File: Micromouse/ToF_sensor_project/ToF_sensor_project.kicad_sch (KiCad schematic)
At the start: 6 parts, among them J3 Conn_01x03_Pin

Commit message: Schematic overhaul
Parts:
- removed C2: 22 µF, Capacitor_SMD:C_0402_1005Metric, symbol Device:C
- removed Cin_VR1: 10 µF, Capacitor_SMD:C_0402_1005Metric, symbol Device:C
- removed J3: Conn_01x03_Pin, Connector_JST:JST_ZH_B3B-ZR_1x03_P1.50mm_Vertical, symbol Connector:Conn_01x03_Pin
- removed Renb1: 30kΩ, Resistor_SMD:R_0603_1608Metric, symbol Device:R
- removed Rent1: 62kΩ, Resistor_SMD:R_0603_1608Metric, symbol Device:R
- removed VR1: TPSM861253RDXR, MM_TPSM861253RDXR:TPSM861253RDXR, symbol TPSM861253RDXR:TPSM861253RDXR
- added C11: 100n, Capacitor_SMD:C_0603_1608Metric, symbol Device:C
- added C9: 4.7u, Capacitor_SMD:C_0603_1608Metric, symbol Device:C
- added J2: Conn_01x06_Pin, symbol Connector:Conn_01x06_Pin
- added R3, R4: 10k, Resistor_SMD:R_0603_1608Metric, symbol Device:R
- added U1: VL53L1CXV0FY1, MM_VL53L4CDV0DH-1:LGA12_STM, symbol Sensor_Distance:VL53L1CXV0FY1
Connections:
- net GND: now also C11.1, C9.1, J2.6 (Pin_6), U1.12 (GND), U1.2 (AVSSVCSEL), U1.3 (GND), U1.4 (GND), U1.6 (GND)
- new net: J2.4 (Pin_4), U1.10 (SCL)
- new net: J2.5 (Pin_5), R4.2, U1.5 (XSHUT)
- new net: J2.2 (Pin_2), R3.2, U1.7 (GPIO1)
- new net: J2.3 (Pin_3), U1.9 (SDA)
- new net +3.3V: C11.2, C9.2, J2.1 (Pin_1), R3.1, R4.1, U1.1 (AVDDVCSEL), U1.11 (AVDD)
- no-connect marks 1 -> 0
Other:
- note added: "+3.3V INT SDA SCL XSHUT GND"
- note added: "I2C lines are pulled up on main schematic"

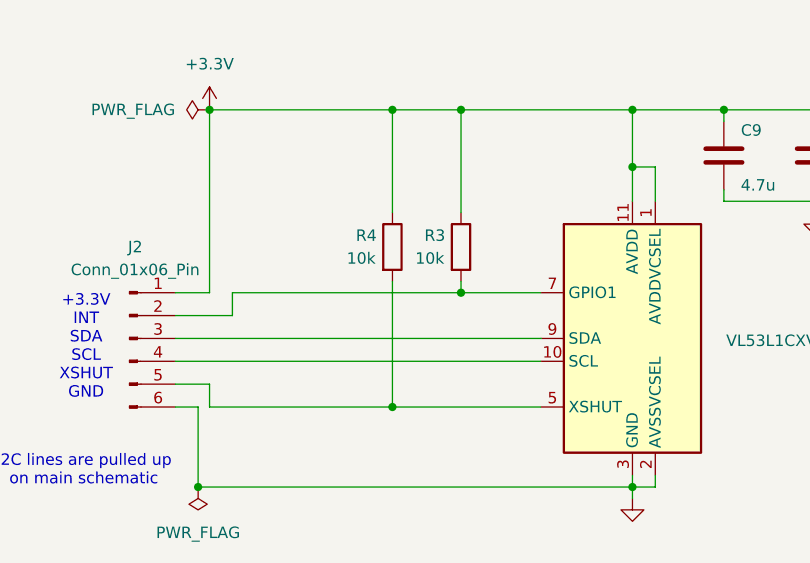
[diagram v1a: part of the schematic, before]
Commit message: Cleaned up layout
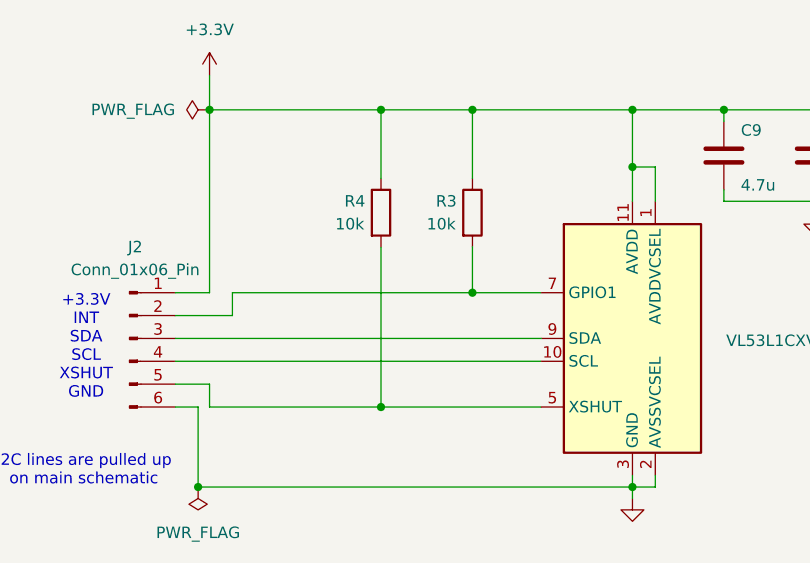
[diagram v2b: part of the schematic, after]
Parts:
- J2: footprint (none) -> Connector_PinHeader_2.00mm:PinHeader_1x06_P2.00mm_Vertical
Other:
- moved on the sheet: R3, R4
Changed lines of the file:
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@@
-	)
-	(junction
-		(at 86.36 77.47)
-		(diameter 0)
-		(color 0 0 0 0)
 	)
 	(junction
@@
 	)
 	(junction
-		(at 93.98 64.77)
+		(at 85.09 44.45)
 		(diameter 0)
 		(color 0 0 0 0)
@@
 	)
 	(junction
+		(at 85.09 77.47)
+		(diameter 0)
+		(color 0 0 0 0)
+	)
+	(junction
 		(at 113.03 86.36)
 		(diameter 0)
@@
 	)
 	(junction
-		(at 93.98 44.45)
+		(at 95.25 64.77)
 		(diameter 0)
 		(color 0 0 0 0)
 	)
 	(junction
-		(at 86.36 44.45)
+		(at 95.25 44.45)
 		(diameter 0)
 		(color 0 0 0 0)
@@
 	(wire
 		(pts
+			(xy 85.09 44.45) (xy 95.25 44.45)
+		)
+		(stroke
+			(width 0)
+			(type default)
+		)
+	)
+	(wire
+		(pts
 			(xy 133.35 53.34) (xy 133.35 54.61)
 		)
@@
 	(wire
 		(pts
-			(xy 93.98 63.5) (xy 93.98 64.77)
+			(xy 95.25 59.69) (xy 95.25 64.77)
 		)
 		(stroke
@@
 	(wire
 		(pts
+			(xy 85.09 77.47) (xy 102.87 77.47)
+		)
+		(stroke
+			(width 0)
+			(type default)
+		)
+	)
+	(wire
+		(pts
 			(xy 115.57 86.36) (xy 115.57 85.09)
 		)
@@
 	(wire
 		(pts
+			(xy 95.25 64.77) (xy 102.87 64.77)
+		)
+		(stroke
+			(width 0)
+			(type default)
+		)
+	)
+	(wire
+		(pts
 			(xy 66.04 64.77) (xy 62.23 64.77)
 		)
@@
 	(wire
 		(pts
-			(xy 66.04 77.47) (xy 86.36 77.47)
+			(xy 66.04 77.47) (xy 85.09 77.47)
 		)
 		(stroke
@@
 	(wire
 		(pts
-			(xy 86.36 77.47) (xy 102.87 77.47)
-		)
-		(stroke
-			(width 0)
-			(type default)
-		)
-	)
-	(wire
-		(pts
-			(xy 86.36 44.45) (xy 113.03 44.45)
-		)
-		(stroke
-			(width 0)
-			(type default)
-		)
-	)
-	(wire
-		(pts
-			(xy 93.98 64.77) (xy 102.87 64.77)
-		)
-		(stroke
-			(width 0)
-			(type default)
-		)
-	)
-	(wire
-		(pts
 			(xy 62.23 69.85) (xy 102.87 69.85)
 		)
@@
 	(wire
 		(pts
-			(xy 68.58 64.77) (xy 93.98 64.77)
-		)
-		(stroke
-			(width 0)
-			(type default)
-		)
-	)
-	(wire
-		(pts
-			(xy 93.98 44.45) (xy 93.98 55.88)
+			(xy 68.58 64.77) (xy 95.25 64.77)
+		)
+		(stroke
+			(width 0)
+			(type default)
+		)
+	)
+	(wire
+		(pts
+			(xy 95.25 44.45) (xy 95.25 52.07)
 		)
 		(stroke
@@
 	(wire
 		(pts
+			(xy 66.04 40.64) (xy 66.04 44.45)
+		)
+		(stroke
+			(width 0)
+			(type default)
+		)
+	)
+	(wire
+		(pts
 			(xy 123.19 44.45) (xy 133.35 44.45)
 		)
@@
 	(wire
 		(pts
-			(xy 66.04 44.45) (xy 86.36 44.45)
+			(xy 66.04 44.45) (xy 85.09 44.45)
+		)
+		(stroke
+			(width 0)
+			(type default)
+		)
+	)
+	(wire
+		(pts
+			(xy 95.25 44.45) (xy 113.03 44.45)
 		)
 		(stroke
@@
 	(wire
 		(pts
-			(xy 86.36 63.5) (xy 86.36 77.47)
+			(xy 85.09 59.69) (xy 85.09 77.47)
 		)
 		(stroke
@@
 	(wire
 		(pts
-			(xy 86.36 44.45) (xy 86.36 55.88)
+			(xy 85.09 44.45) (xy 85.09 52.07)
 		)
 		(stroke
@@
 	(symbol
 		(lib_id "power:+3.3V")
-		(at 66.04 44.45 0)
+		(at 66.04 40.64 0)
 		(unit 1)
 		(body_style 1)
@@
 		(fields_autoplaced yes)
 		(property "Reference" "#PWR01"
-			(at 66.04 48.26 0)
+			(at 66.04 44.45 0)
 			(hide yes)
 			(show_name no)
@@
 		)
 		(property "Value" "+3.3V"
-			(at 66.04 39.37 0)
+			(at 66.04 35.56 0)
 			(show_name no)
 			(do_not_autoplace no)
@@
 		)
 		(property "Footprint" ""
-			(at 66.04 44.45 0)
+			(at 66.04 40.64 0)
 			(hide yes)
 			(show_name no)
@@
 		)
 		(property "Datasheet" ""
-			(at 66.04 44.45 0)
+			(at 66.04 40.64 0)
 			(hide yes)
 			(show_name no)
@@
 		)
 		(property "Description" "Power symbol creates a global label with name \"+3.3V\""
-			(at 66.04 44.45 0)
+			(at 66.04 40.64 0)
 			(hide yes)
 			(show_name no)
@@
 	(symbol
 		(lib_id "Device:R")
-		(at 93.98 59.69 0)
+		(at 95.25 55.88 0)
 		(unit 1)
 		(body_style 1)
@@
 		(dnp no)
 		(property "Reference" "R3"
-			(at 89.916 58.42 0)
+			(at 91.186 54.61 0)
 			(show_name no)
 			(do_not_autoplace no)
@@
 		)
 		(property "Value" "10k"
-			(at 88.9 60.96 0)
+			(at 90.17 57.15 0)
 			(show_name no)
 			(do_not_autoplace no)
@@
 		)
 		(property "Footprint" "Resistor_SMD:R_0603_1608Metric"
-			(at 92.202 59.69 90)
+			(at 93.472 55.88 90)
 			(hide yes)
 			(show_name no)
@@
 		)
 		(property "Datasheet" ""
-			(at 93.98 59.69 0)
+			(at 95.25 55.88 0)
 			(hide yes)
 			(show_name no)
@@
 		)
 		(property "Description" "Resistor"
-			(at 93.98 59.69 0)
+			(at 95.25 55.88 0)
 			(hide yes)
 			(show_name no)
@@
 		)
 		(property "Availability" ""
-			(at 93.98 59.69 0)
+			(at 95.25 55.88 0)
 			(hide yes)
 			(show_name no)
@@
 		)
 		(property "Check_prices" ""
-			(at 93.98 59.69 0)
+			(at 95.25 55.88 0)
 			(hide yes)
 			(show_name no)
@@
 		)
 		(property "Description_1" ""
-			(at 93.98 59.69 0)
+			(at 95.25 55.88 0)
 			(hide yes)
 			(show_name no)
@@
 		)
 		(property "MF" ""
-			(at 93.98 59.69 0)
+			(at 95.25 55.88 0)
 			(hide yes)
 			(show_name no)
@@
 		)
 		(property "MP" ""
-			(at 93.98 59.69 0)
+			(at 95.25 55.88 0)
 			(hide yes)
 			(show_name no)
@@
 		)
 		(property "Package" ""
-			(at 93.98 59.69 0)
+			(at 95.25 55.88 0)
 			(hide yes)
 			(show_name no)
@@
 		)
 		(property "Price" ""
-			(at 93.98 59.69 0)
+			(at 95.25 55.88 0)
 			(hide yes)
 			(show_name no)
@@
 		)
 		(property "SnapEDA_Link" ""
-			(at 93.98 59.69 0)
+			(at 95.25 55.88 0)
 			(hide yes)
 			(show_name no)
@@
 	(symbol
 		(lib_id "Device:R")
-		(at 86.36 59.69 0)
+		(at 85.09 55.88 0)
 		(unit 1)
 		(body_style 1)
@@
 		(dnp no)
 		(property "Reference" "R4"
-			(at 82.296 58.42 0)
+			(at 81.026 54.61 0)
 			(show_name no)
 			(do_not_autoplace no)
@@
 		)
 		(property "Value" "10k"
-			(at 81.28 60.96 0)
+			(at 80.01 57.15 0)
 			(show_name no)
 			(do_not_autoplace no)
@@
 		)
 		(property "Footprint" "Resistor_SMD:R_0603_1608Metric"
-			(at 84.582 59.69 90)
+			(at 83.312 55.88 90)
 			(hide yes)
 			(show_name no)
@@
 		)
 		(property "Datasheet" ""
-			(at 86.36 59.69 0)
+			(at 85.09 55.88 0)
 			(hide yes)
 			(show_name no)
@@
 		)
 		(property "Description" "Resistor"
-			(at 86.36 59.69 0)
+			(at 85.09 55.88 0)
 			(hide yes)
 			(show_name no)
@@
 		)
 		(property "Availability" ""
-			(at 86.36 59.69 0)
+			(at 85.09 55.88 0)
 			(hide yes)
 			(show_name no)
@@
 		)
 		(property "Check_prices" ""
-			(at 86.36 59.69 0)
+			(at 85.09 55.88 0)
 			(hide yes)
 			(show_name no)
@@
 		)
 		(property "Description_1" ""
-			(at 86.36 59.69 0)
+			(at 85.09 55.88 0)
 			(hide yes)
 			(show_name no)
@@
 		)
 		(property "MF" ""
-			(at 86.36 59.69 0)
+			(at 85.09 55.88 0)
 			(hide yes)
 			(show_name no)
@@
 		)
 		(property "MP" ""
-			(at 86.36 59.69 0)
+			(at 85.09 55.88 0)
 			(hide yes)
 			(show_name no)
@@
 		)
 		(property "Package" ""
-			(at 86.36 59.69 0)
+			(at 85.09 55.88 0)
 			(hide yes)
 			(show_name no)
@@
 		)
 		(property "Price" ""
-			(at 86.36 59.69 0)
+			(at 85.09 55.88 0)
 			(hide yes)
 			(show_name no)
@@
 		)
 		(property "SnapEDA_Link" ""
-			(at 86.36 59.69 0)
+			(at 85.09 55.88 0)
 			(hide yes)
 			(show_name no)
@@
 			)
 		)
-		(property "Footprint" ""
+		(property "Footprint" "Connector_PinHeader_2.00mm:PinHeader_1x06_P2.00mm_Vertical"
 			(at 57.15 69.85 0)
 			(hide yes)

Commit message: Completed IR board, ToF board, changed IMU
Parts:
- J1: renamed from J2; footprint Connector_PinHeader_2.00mm:PinHeader_1x06_P2.00mm_Vertical -> Connector_PinHeader_2.00mm:PinHeader_1x06_P2.00mm_Horizontal
- U1: footprint MM_VL53L4CDV0DH-1:LGA12_STM -> Sensor_Distance:ST_VL53L1x
- renumbered C9 to C1, C11 to C2, R4 to R1, R3 to R2
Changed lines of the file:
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@@
 		(in_pos_files yes)
 		(dnp no)
-		(property "Reference" "C11"
+		(property "Reference" "C2"
 			(at 137.16 46.482 0)
 			(show_name no)
@@
 			(project "ToF_sensor_project"
 				(path "/a78c32f3-225d-44b3-9e1d-ab79a557afd0"
-					(reference "C11")
+					(reference "C2")
 					(unit 1)
 				)
@@
 			)
 		)
-		(property "Footprint" "MM_VL53L4CDV0DH-1:LGA12_STM"
+		(property "Footprint" "Sensor_Distance:ST_VL53L1x"
 			(at 130.175 83.82 0)
 			(hide yes)
@@
 		(dnp no)
 		(fields_autoplaced yes)
-		(property "Reference" "#PWR013"
+		(property "Reference" "#PWR03"
 			(at 133.35 62.23 0)
 			(hide yes)
@@
 			(project "ToF_sensor_project"
 				(path "/a78c32f3-225d-44b3-9e1d-ab79a557afd0"
-					(reference "#PWR013")
+					(reference "#PWR03")
 					(unit 1)
 				)
@@
 		(in_pos_files yes)
 		(dnp no)
-		(property "Reference" "R3"
+		(property "Reference" "R2"
 			(at 91.186 54.61 0)
 			(show_name no)
@@
 			(project "ToF_sensor_project"
 				(path "/a78c32f3-225d-44b3-9e1d-ab79a557afd0"
-					(reference "R3")
+					(reference "R2")
 					(unit 1)
 				)
@@
 		(in_pos_files yes)
 		(dnp no)
-		(property "Reference" "R4"
+		(property "Reference" "R1"
 			(at 81.026 54.61 0)
 			(show_name no)
@@
 			(project "ToF_sensor_project"
 				(path "/a78c32f3-225d-44b3-9e1d-ab79a557afd0"
-					(reference "R4")
+					(reference "R1")
 					(unit 1)
 				)
@@
 		(dnp no)
 		(fields_autoplaced yes)
-		(property "Reference" "J2"
+		(property "Reference" "J1"
 			(at 57.785 59.69 0)
 			(show_name no)
@@
 			)
 		)
-		(property "Footprint" "Connector_PinHeader_2.00mm:PinHeader_1x06_P2.00mm_Vertical"
+		(property "Footprint" "Connector_PinHeader_2.00mm:PinHeader_1x06_P2.00mm_Horizontal"
 			(at 57.15 69.85 0)
 			(hide yes)
@@
 			(project "ToF_sensor_project"
 				(path "/a78c32f3-225d-44b3-9e1d-ab79a557afd0"
-					(reference "J2")
+					(reference "J1")
 					(unit 1)
 				)
@@
 		(dnp no)
 		(fields_autoplaced yes)
-		(property "Reference" "#FLG01"
+		(property "Reference" "#FLG02"
 			(at 64.135 44.45 0)
 			(hide yes)
@@
 			(project "ToF_sensor_project"
 				(path "/a78c32f3-225d-44b3-9e1d-ab79a557afd0"
-					(reference "#FLG01")
+					(reference "#FLG02")
 					(unit 1)
 				)
@@
 		(dnp no)
 		(fields_autoplaced yes)
-		(property "Reference" "#FLG02"
+		(property "Reference" "#FLG01"
 			(at 64.77 88.265 0)
 			(hide yes)
@@
 			(project "ToF_sensor_project"
 				(path "/a78c32f3-225d-44b3-9e1d-ab79a557afd0"
-					(reference "#FLG02")
+					(reference "#FLG01")
 					(unit 1)
 				)
@@
 		(dnp no)
 		(fields_autoplaced yes)
-		(property "Reference" "#PWR014"
+		(property "Reference" "#PWR02"
 			(at 113.03 93.98 0)
 			(hide yes)
@@
 			(project "ToF_sensor_project"
 				(path "/a78c32f3-225d-44b3-9e1d-ab79a557afd0"
-					(reference "#PWR014")
+					(reference "#PWR02")
 					(unit 1)
 				)
@@
 		(in_pos_files yes)
 		(dnp no)
-		(property "Reference" "C9"
+		(property "Reference" "C1"
 			(at 126.238 46.736 0)
 			(show_name no)
@@
 			(project "ToF_sensor_project"
 				(path "/a78c32f3-225d-44b3-9e1d-ab79a557afd0"
-					(reference "C9")
+					(reference "C1")
 					(unit 1)
 				)
